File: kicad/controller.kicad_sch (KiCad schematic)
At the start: 25 parts, among them U1 RP2040, U2 W25Q16JVUXIQ, Y1 Crystal_GND24

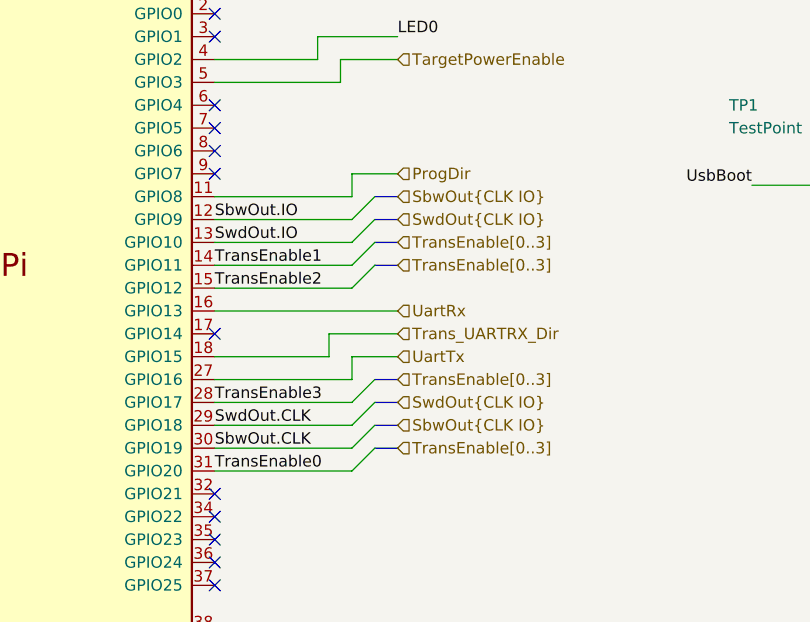
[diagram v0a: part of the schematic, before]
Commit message: add fourth level converter for simultaneous programming + TX/RX
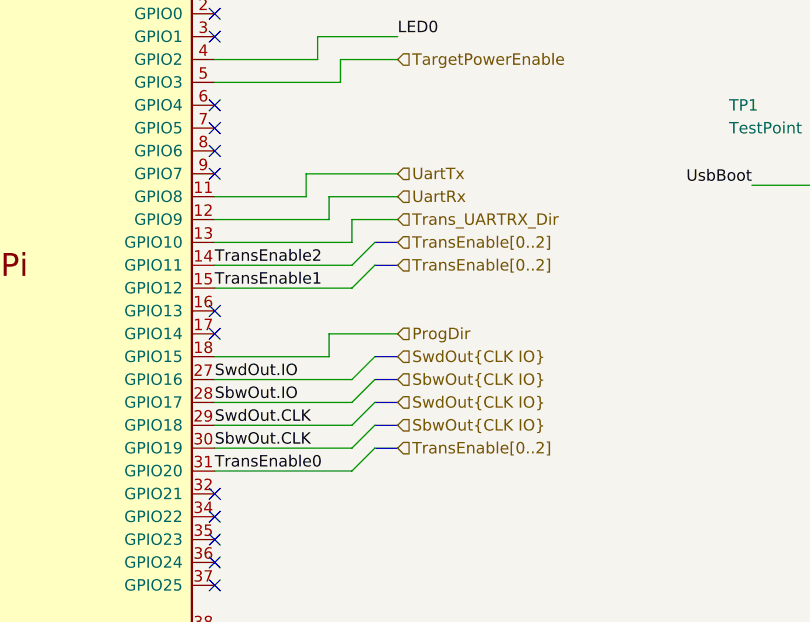
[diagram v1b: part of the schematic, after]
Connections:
- net TransEnable3 is gone; now on net SbwOut.IO: U1.28 (GPIO17)
- net ProgDir: now also U1.18 (GPIO15); no longer U1.11 (GPIO8)
- net SbwOut.IO: no longer U1.12 (GPIO9)
- net SwdOut.IO: now also U1.27 (GPIO16); no longer U1.13 (GPIO10)
- net TransEnable1: now also U1.15 (GPIO12); no longer U1.14 (GPIO11)
- net TransEnable2: now also U1.14 (GPIO11); no longer U1.15 (GPIO12)
- net Trans_UARTRX_Dir: now also U1.13 (GPIO10); no longer U1.18 (GPIO15)
- net UartRx: now also U1.12 (GPIO9); no longer U1.16 (GPIO13)
- net UartTx: now also U1.11 (GPIO8); no longer U1.27 (GPIO16)
- no-connect marks 19 -> 20

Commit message: replace target supply diode with analog switch
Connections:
- net LED0: now also U1.3 (GPIO1); no longer U1.4 (GPIO2)
- net TargetPowerEnable: now also U1.4 (GPIO2); no longer U1.5 (GPIO3)
- net PiGpio2: now reaches U1.37 (GPIO25)
- net PiGpio3: now reaches U1.38 (GPIO26_ADC0)
- net PiGpio0: now reaches U1.6 (GPIO4)
- net PiGpio1: now reaches U1.8 (GPIO6)
- no-connect marks 20 -> 16
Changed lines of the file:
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@@
   (junction (at 135.89 62.23) (diameter 0) (color 0 0 0 0)
   )
-  (no_connect (at 151.13 97.79))
   (no_connect (at 151.13 166.37))
-  (no_connect (at 151.13 110.49))
+  (no_connect (at 151.13 113.03))
   (no_connect (at 151.13 107.95))
   (no_connect (at 87.63 162.56))
@@
   (no_connect (at 151.13 148.59))
   (no_connect (at 151.13 171.45))
-  (no_connect (at 151.13 163.83))
   (no_connect (at 87.63 148.59))
-  (no_connect (at 151.13 113.03))
   (no_connect (at 87.63 160.02))
   (no_connect (at 151.13 153.67))
   (no_connect (at 151.13 95.25))
+  (no_connect (at 151.13 102.87))
   (no_connect (at 151.13 168.91))
   (no_connect (at 151.13 151.13))
-  (no_connect (at 151.13 158.75))
-  (no_connect (at 151.13 105.41))
   (no_connect (at 151.13 128.27))
   (no_connect (at 151.13 156.21))
@@
     (stroke (width 0) (type default) (color 0 0 0 0))
   )
+  (bus_entry (at 168.91 156.21) (size -2.54 2.54)
+    (stroke (width 0) (type default) (color 0 0 0 0))
+  )
   (bus_entry (at 168.91 120.65) (size -2.54 2.54)
     (stroke (width 0) (type default) (color 0 0 0 0))
   )
+  (bus_entry (at 168.91 107.95) (size -2.54 2.54)
+    (stroke (width 0) (type default) (color 0 0 0 0))
+  )
   (bus_entry (at 168.91 123.19) (size -2.54 2.54)
     (stroke (width 0) (type default) (color 0 0 0 0))
@@
     (stroke (width 0) (type default) (color 0 0 0 0))
   )
+  (bus_entry (at 168.91 161.29) (size -2.54 2.54)
+    (stroke (width 0) (type default) (color 0 0 0 0))
+  )
+  (bus_entry (at 168.91 102.87) (size -2.54 2.54)
+    (stroke (width 0) (type default) (color 0 0 0 0))
+  )
   (bus_entry (at 168.91 138.43) (size -2.54 2.54)
     (stroke (width 0) (type default) (color 0 0 0 0))
@@
     (stroke (width 0) (type default) (color 0 0 0 0))
   )
+  (wire (pts (xy 151.13 158.75) (xy 166.37 158.75))
+    (stroke (width 0) (type default) (color 0 0 0 0))
+  )
   (wire (pts (xy 166.37 118.11) (xy 171.45 118.11))
     (stroke (width 0) (type default) (color 0 0 0 0))
@@
     (stroke (width 0) (type default) (color 0 0 0 0))
   )
-  (wire (pts (xy 162.56 97.79) (xy 162.56 100.33))
-    (stroke (width 0) (type default) (color 0 0 0 0))
-  )
   (wire (pts (xy 101.6 77.47) (xy 101.6 68.58))
     (stroke (width 0) (type default) (color 0 0 0 0))
@@
     (stroke (width 0) (type default) (color 0 0 0 0))
   )
+  (wire (pts (xy 151.13 163.83) (xy 166.37 163.83))
+    (stroke (width 0) (type default) (color 0 0 0 0))
+  )
   (wire (pts (xy 256.54 95.25) (xy 256.54 106.68))
     (stroke (width 0) (type default) (color 0 0 0 0))
@@
     (stroke (width 0) (type default) (color 0 0 0 0))
   )
+  (wire (pts (xy 151.13 110.49) (xy 166.37 110.49))
+    (stroke (width 0) (type default) (color 0 0 0 0))
+  )
   (wire (pts (xy 43.18 129.54) (xy 39.37 129.54))
     (stroke (width 0) (type default) (color 0 0 0 0))
@@
     (stroke (width 0) (type default) (color 0 0 0 0))
   )
+  (wire (pts (xy 151.13 100.33) (xy 171.45 100.33))
+    (stroke (width 0) (type default) (color 0 0 0 0))
+  )
   (wire (pts (xy 151.13 135.89) (xy 166.37 135.89))
     (stroke (width 0) (type default) (color 0 0 0 0))
@@
     (stroke (width 0) (type default) (color 0 0 0 0))
   )
+  (bus (pts (xy 168.91 102.87) (xy 171.45 102.87))
+    (stroke (width 0) (type default) (color 0 0 0 0))
+  )
   (wire (pts (xy 152.4 57.15) (xy 152.4 58.42))
     (stroke (width 0) (type default) (color 0 0 0 0))
@@
     (stroke (width 0) (type default) (color 0 0 0 0))
   )
+  (bus (pts (xy 168.91 156.21) (xy 168.91 161.29))
+    (stroke (width 0) (type default) (color 0 0 0 0))
+  )
   (wire (pts (xy 123.19 69.85) (xy 125.73 69.85))
     (stroke (width 0) (type default) (color 0 0 0 0))
@@
     (stroke (width 0) (type default) (color 0 0 0 0))
   )
+  (wire (pts (xy 151.13 97.79) (xy 171.45 97.79))
+    (stroke (width 0) (type default) (color 0 0 0 0))
+  )
   (wire (pts (xy 241.3 114.3) (xy 243.84 114.3))
     (stroke (width 0) (type default) (color 0 0 0 0))
@@
     (stroke (width 0) (type default) (color 0 0 0 0))
   )
-  (wire (pts (xy 151.13 102.87) (xy 165.1 102.87))
-    (stroke (width 0) (type default) (color 0 0 0 0))
-  )
   (bus (pts (xy 168.91 133.35) (xy 171.45 133.35))
     (stroke (width 0) (type default) (color 0 0 0 0))
@@
     (stroke (width 0) (type default) (color 0 0 0 0))
   )
-  (wire (pts (xy 171.45 97.79) (xy 162.56 97.79))
-    (stroke (width 0) (type default) (color 0 0 0 0))
-  )
   (wire (pts (xy 246.38 46.99) (xy 246.38 48.26))
     (stroke (width 0) (type default) (color 0 0 0 0))
@@
     (stroke (width 0) (type default) (color 0 0 0 0))
   )
+  (bus (pts (xy 168.91 156.21) (xy 171.45 156.21))
+    (stroke (width 0) (type default) (color 0 0 0 0))
+  )
   (wire (pts (xy 228.6 114.3) (xy 241.3 114.3))
     (stroke (width 0) (type default) (color 0 0 0 0))
@@
     (stroke (width 0) (type default) (color 0 0 0 0))
   )
-  (wire (pts (xy 151.13 100.33) (xy 162.56 100.33))
-    (stroke (width 0) (type default) (color 0 0 0 0))
-  )
   (wire (pts (xy 163.83 130.81) (xy 163.83 133.35))
     (stroke (width 0) (type default) (color 0 0 0 0))
@@
     (stroke (width 0) (type default) (color 0 0 0 0))
   )
-  (wire (pts (xy 171.45 100.33) (xy 165.1 100.33))
-    (stroke (width 0) (type default) (color 0 0 0 0))
-  )
   (bus (pts (xy 168.91 138.43) (xy 171.45 138.43))
     (stroke (width 0) (type default) (color 0 0 0 0))
@@
     (stroke (width 0) (type default) (color 0 0 0 0))
   )
+  (bus (pts (xy 168.91 102.87) (xy 168.91 107.95))
+    (stroke (width 0) (type default) (color 0 0 0 0))
+  )
   (wire (pts (xy 203.2 48.26) (xy 193.04 48.26))
     (stroke (width 0) (type default) (color 0 0 0 0))
@@
     (stroke (width 0) (type default) (color 0 0 0 0))
   )
+  (wire (pts (xy 151.13 105.41) (xy 166.37 105.41))
+    (stroke (width 0) (type default) (color 0 0 0 0))
+  )
   (wire (pts (xy 82.55 107.95) (xy 87.63 107.95))
     (stroke (width 0) (type default) (color 0 0 0 0))
@@
     (stroke (width 0) (type default) (color 0 0 0 0))
   )
-  (wire (pts (xy 165.1 100.33) (xy 165.1 102.87))
-    (stroke (width 0) (type default) (color 0 0 0 0))
-  )
   (wire (pts (xy 162.56 58.42) (xy 172.72 58.42))
     (stroke (width 0) (type default) (color 0 0 0 0))
@@
     (effects (font (size 1.27 1.27)) (justify right bottom))
   )
+  (label "PiGpio3" (at 151.13 163.83 0)
+    (effects (font (size 1.27 1.27)) (justify left bottom))
+  )
+  (label "PiGpio0" (at 151.13 105.41 0)
+    (effects (font (size 1.27 1.27)) (justify left bottom))
+  )
   (label "TransEnable0" (at 151.13 146.05 0)
     (effects (font (size 1.27 1.27)) (justify left bottom))
@@
     (effects (font (size 1.27 1.27)) (justify right bottom))
   )
+  (label "PiGpio2" (at 151.13 158.75 0)
+    (effects (font (size 1.27 1.27)) (justify left bottom))
+  )
   (label "QSPI_SD0" (at 82.55 100.33 180)
     (effects (font (size 1.27 1.27)) (justify right bottom))
@@
     (effects (font (size 1.27 1.27)) (justify right bottom))
   )
+  (label "PiGpio1" (at 151.13 110.49 0)
+    (effects (font (size 1.27 1.27)) (justify left bottom))
+  )
+  (hierarchical_label "PiGpio[0..3]" (shape input) (at 171.45 102.87 0)
+    (effects (font (size 1.27 1.27)) (justify left))
+  )
   (hierarchical_label "UartTx" (shape input) (at 171.45 113.03 0)
     (effects (font (size 1.27 1.27)) (justify left))
@@
     (effects (font (size 1.27 1.27)) (justify left))
   )
+  (hierarchical_label "PiGpio[0..3]" (shape input) (at 171.45 156.21 0)
+    (effects (font (size 1.27 1.27)) (justify left))
+  )

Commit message: add MPNs in schematics
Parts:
- C1, C2: MPN (none) -> 04025A120JAT2A
- C10, C11, C12, C13, C14, C3, C4, C6, C8, C9: MPN (none) -> CL05A104KA5NNNC
- C5, C7: MPN (none) -> CL05A475MP5NRNC
- D1: MPN (none) -> QBLP595-AG1
- R1, R4: MPN (none) -> WR04X1001FTL
- R2, R3: MPN (none) -> CR0402-FX-27R0GLF
- R6: MPN (none) -> CR0402-FX-1200GLF
- U1: MPN (none) -> RP2040-7
- U2: MPN (none) -> W25Q16JVUXIQ
- Y1: MPN (none) -> RH100-12.000-18-2030-TR
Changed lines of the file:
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@@
+      (effects (font (size 1.27 1.27)) hide)
+    )
+    (property "MPN" "CL05A104KA5NNNC" (id 4) (at 142.24 53.34 0)
       (effects (font (size 1.27 1.27)) hide)
     )
@@
       (effects (font (size 1.27 1.27)) hide)
     )
+    (property "MPN" "CR0402-FX-27R0GLF" (id 4) (at 166.37 87.63 0)
+      (effects (font (size 1.27 1.27)) hide)
+    )
     (pin "1")
     (pin "2")
@@
     )
     (property "Datasheet" "~" (id 3) (at 246.38 52.07 0)
+      (effects (font (size 1.27 1.27)) hide)
+    )
+    (property "MPN" "QBLP595-AG1" (id 4) (at 246.38 52.07 0)
       (effects (font (size 1.27 1.27)) hide)
     )
@@
       (effects (font (size 1.27 1.27)) hide)
     )
+    (property "MPN" "RH100-12.000-18-2030-TR" (id 4) (at 48.26 129.54 0)
+      (effects (font (size 1.27 1.27)) hide)
+    )
     (pin "1")
     (pin "2")
@@
     )
     (property "Datasheet" "" (id 3) (at 100.33 128.27 0)
+      (effects (font (size 1.27 1.27)) hide)
+    )
+    (property "MPN" "RP2040-7" (id 4) (at 119.38 128.27 0)
       (effects (font (size 1.27 1.27)) hide)
     )
@@
       (effects (font (size 1.27 1.27)) hide)
     )
+    (property "MPN" "CL05A104KA5NNNC" (id 4) (at 81.28 53.34 0)
+      (effects (font (size 1.27 1.27)) hide)
+    )
     (pin "1")
     (pin "2")
@@
     )
     (property "Datasheet" "~" (id 3) (at 91.44 53.34 0)
+      (effects (font (size 1.27 1.27)) hide)
+    )
+    (property "MPN" "CL05A104KA5NNNC" (id 4) (at 91.44 53.34 0)
       (effects (font (size 1.27 1.27)) hide)
     )
@@
       (effects (font (size 1.27 1.27)) hide)
     )
+    (property "MPN" "CL05A104KA5NNNC" (id 4) (at 193.04 53.34 0)
+      (effects (font (size 1.27 1.27)) hide)
+    )
     (pin "1")
     (pin "2")
@@
       (effects (font (size 1.27 1.27)) hide)
     )
+    (property "MPN" "04025A120JAT2A" (id 4) (at 31.75 123.19 0)
+      (effects (font (size 1.27 1.27)) hide)
+    )
     (pin "1")
     (pin "2")
@@
     )
     (property "Datasheet" "~" (id 3) (at 91.44 67.31 0)
+      (effects (font (size 1.27 1.27)) hide)
+    )
+    (property "MPN" "CL05A475MP5NRNC" (id 4) (at 91.44 67.31 0)
       (effects (font (size 1.27 1.27)) hide)
     )
@@
     )
     (property "Datasheet" "https://www.winbond.com/resource-files/w25q16jv%20spi%20revh%2004082019%20plus.pdf" (id 3) (at 257.81 139.7 0)
+      (effects (font (size 1.27 1.27)) hide)
+    )
+    (property "MPN" "W25Q16JVUXIQ" (id 4) (at 256.54 116.84 0)
       (effects (font (size 1.27 1.27)) hide)
     )
@@
       (effects (font (size 1.27 1.27)) hide)
     )
+    (property "MPN" "CL05A104KA5NNNC" (id 4) (at 172.72 53.34 0)
+      (effects (font (size 1.27 1.27)) hide)
+    )
     (pin "1")
     (pin "2")
@@
     )
     (property "Datasheet" "~" (id 3) (at 162.56 53.34 0)
+      (effects (font (size 1.27 1.27)) hide)
+    )
+    (property "MPN" "CL05A104KA5NNNC" (id 4) (at 162.56 53.34 0)
       (effects (font (size 1.27 1.27)) hide)
     )
@@
       (effects (font (size 1.27 1.27)) hide)
     )
+    (property "MPN" "WR04X1001FTL" (id 4) (at 224.79 114.3 0)
+      (effects (font (size 1.27 1.27)) hide)
+    )
     (pin "1")
     (pin "2")
@@
       (effects (font (size 1.27 1.27)) hide)
     )
+    (property "MPN" "04025A120JAT2A" (id 4) (at 31.75 135.89 0)
+      (effects (font (size 1.27 1.27)) hide)
+    )
     (pin "1")
     (pin "2")
@@
       (effects (font (size 1.27 1.27)) hide)
     )
+    (property "MPN" "CL05A104KA5NNNC" (id 4) (at 182.88 53.34 0)
+      (effects (font (size 1.27 1.27)) hide)
+    )
     (pin "1")
     (pin "2")
@@
       (effects (font (size 1.27 1.27)) hide)
     )
+    (property "MPN" "CL05A104KA5NNNC" (id 4) (at 262.89 96.52 0)
+      (effects (font (size 1.27 1.27)) hide)
+    )
     (pin "1")
     (pin "2")
@@
     )
     (property "Datasheet" "~" (id 3) (at 142.24 67.31 0)
+      (effects (font (size 1.27 1.27)) hide)
+    )
+    (property "MPN" "CL05A475MP5NRNC" (id 4) (at 142.24 67.31 0)
       (effects (font (size 1.27 1.27)) hide)
     )
@@
       (effects (font (size 1.27 1.27)) hide)
     )
+    (property "MPN" "WR04X1001FTL" (id 4) (at 68.58 135.89 0)
+      (effects (font (size 1.27 1.27)) hide)
+    )
     (pin "1")
     (pin "2")
@@
     )
     (property "Datasheet" "~" (id 3) (at 246.38 43.18 0)
+      (effects (font (size 1.27 1.27)) hide)
+    )
+    (property "MPN" "CR0402-FX-1200GLF" (id 4) (at 246.38 43.18 0)
       (effects (font (size 1.27 1.27)) hide)
     )
@@
       (effects (font (size 1.27 1.27)) hide)
     )
+    (property "MPN" "CR0402-FX-27R0GLF" (id 4) (at 166.37 78.74 0)
+      (effects (font (size 1.27 1.27)) hide)
+    )
     (pin "1")
     (pin "2")
@@
       (effects (font (size 1.27 1.27)) hide)
     )
+    (property "MPN" "CL05A104KA5NNNC" (id 4) (at 152.4 53.34 0)
+      (effects (font (size 1.27 1.27)) hide)
+    )
     (pin "1")
     (pin "2")
@@
       (effects (font (size 1.27 1.27)) hide)
     )
+    (property "MPN" "CL05A104KA5NNNC" (id 4) (at 203.2 53.34 0)
+      (effects (font (size 1.27 1.27)) hide)
+    )

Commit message: update footprints and add component description to BOM
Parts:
- U1: MPN RP2040-7 -> RP2040
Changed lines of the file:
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@@
+      (effects (font (size 1.27 1.27)) hide)
+    )
+    (property "Description" "Cap, 0402, X5R/X7R, 10V" (id 5) (at 142.24 53.34 0)
       (effects (font (size 1.27 1.27)) hide)
     )
@@
       (effects (font (size 1.27 1.27)) hide)
     )
+    (property "Description" "Res, 0402, 1%" (id 5) (at 166.37 87.63 0)
+      (effects (font (size 1.27 1.27)) hide)
+    )
     (pin "1")
     (pin "2")
@@
     )
     (property "MPN" "QBLP595-AG1" (id 4) (at 246.38 52.07 0)
+      (effects (font (size 1.27 1.27)) hide)
+    )
+    (property "Description" "LED, 0402, green, clear" (id 5) (at 246.38 52.07 0)
       (effects (font (size 1.27 1.27)) hide)
     )
@@
       (effects (font (size 1.27 1.27)) hide)
     )
+    (property "Description" "12MHZ 18PF Crystal" (id 5) (at 48.26 129.54 0)
+      (effects (font (size 1.27 1.27)) hide)
+    )
     (pin "1")
     (pin "2")
@@
       (effects (font (size 1.27 1.27)) hide)
     )
-    (property "MPN" "RP2040-7" (id 4) (at 119.38 128.27 0)
+    (property "MPN" "RP2040" (id 4) (at 119.38 128.27 0)
+      (effects (font (size 1.27 1.27)) hide)
+    )
+    (property "Description" "" (id 5) (at 119.38 128.27 0)
       (effects (font (size 1.27 1.27)) hide)
     )
@@
       (effects (font (size 1.27 1.27)) hide)
     )
+    (property "Description" "Cap, 0402, X5R/X7R, 10V" (id 5) (at 81.28 53.34 0)
+      (effects (font (size 1.27 1.27)) hide)
+    )
     (pin "1")
     (pin "2")
@@
     )
     (property "MPN" "CL05A104KA5NNNC" (id 4) (at 91.44 53.34 0)
+      (effects (font (size 1.27 1.27)) hide)
+    )
+    (property "Description" "Cap, 0402, X5R/X7R, 10V" (id 5) (at 91.44 53.34 0)
       (effects (font (size 1.27 1.27)) hide)
     )
@@
       (effects (font (size 1.27 1.27)) hide)
     )
+    (property "Description" "Cap, 0402, X5R/X7R, 10V" (id 5) (at 193.04 53.34 0)
+      (effects (font (size 1.27 1.27)) hide)
+    )
     (pin "1")
     (pin "2")
@@
       (effects (font (size 1.27 1.27)) hide)
     )
+    (property "Description" "Cap, 0402, C0G/NP0, 50V" (id 5) (at 31.75 123.19 0)
+      (effects (font (size 1.27 1.27)) hide)
+    )
     (pin "1")
     (pin "2")
@@
     )
     (property "MPN" "CL05A475MP5NRNC" (id 4) (at 91.44 67.31 0)
+      (effects (font (size 1.27 1.27)) hide)
+    )
+    (property "Description" "Cap, 0402, X5R/X7R, 10V" (id 5) (at 91.44 67.31 0)
       (effects (font (size 1.27 1.27)) hide)
     )
@@
     )
     (property "MPN" "W25Q16JVUXIQ" (id 4) (at 256.54 116.84 0)
+      (effects (font (size 1.27 1.27)) hide)
+    )
+    (property "Description" "16Mbi SPI NOR flash" (id 5) (at 256.54 116.84 0)
       (effects (font (size 1.27 1.27)) hide)
     )
@@
       (effects (font (size 1.27 1.27)) hide)
     )
+    (property "Description" "Cap, 0402, X5R/X7R, 10V" (id 5) (at 172.72 53.34 0)
+      (effects (font (size 1.27 1.27)) hide)
+    )
     (pin "1")
     (pin "2")
@@
     )
     (property "MPN" "CL05A104KA5NNNC" (id 4) (at 162.56 53.34 0)
+      (effects (font (size 1.27 1.27)) hide)
+    )
+    (property "Description" "Cap, 0402, X5R/X7R, 10V" (id 5) (at 162.56 53.34 0)
       (effects (font (size 1.27 1.27)) hide)
     )
@@
       (effects (font (size 1.27 1.27)) hide)
     )
+    (property "Description" "Res, 0402, 1%" (id 5) (at 224.79 114.3 0)
+      (effects (font (size 1.27 1.27)) hide)
+    )
     (pin "1")
     (pin "2")
@@
       (effects (font (size 1.27 1.27)) hide)
     )
+    (property "Description" "Cap, 0402, C0G/NP0, 50V" (id 5) (at 31.75 135.89 0)
+      (effects (font (size 1.27 1.27)) hide)
+    )
     (pin "1")
     (pin "2")
@@
       (effects (font (size 1.27 1.27)) hide)
     )
+    (property "Description" "Cap, 0402, X5R/X7R, 10V" (id 5) (at 182.88 53.34 0)
+      (effects (font (size 1.27 1.27)) hide)
+    )
     (pin "1")
     (pin "2")
@@
       (effects (font (size 1.27 1.27)) hide)
     )
+    (property "Description" "Cap, 0402, X5R/X7R, 10V" (id 5) (at 262.89 96.52 0)
+      (effects (font (size 1.27 1.27)) hide)
+    )
     (pin "1")
     (pin "2")
@@
     )
     (property "MPN" "CL05A475MP5NRNC" (id 4) (at 142.24 67.31 0)
+      (effects (font (size 1.27 1.27)) hide)
+    )
+    (property "Description" "Cap, 0402, X5R/X7R, 10V" (id 5) (at 142.24 67.31 0)
       (effects (font (size 1.27 1.27)) hide)
     )
@@
       (effects (font (size 1.27 1.27)) hide)
     )
+    (property "Description" "Res, 0402, 1%" (id 5) (at 68.58 135.89 0)
+      (effects (font (size 1.27 1.27)) hide)
+    )
     (pin "1")
     (pin "2")
@@
     )
     (property "MPN" "CR0402-FX-1200GLF" (id 4) (at 246.38 43.18 0)
+      (effects (font (size 1.27 1.27)) hide)
+    )
+    (property "Description" "Res, 0402, 1%" (id 5) (at 246.38 43.18 0)
       (effects (font (size 1.27 1.27)) hide)
     )
@@
       (effects (font (size 1.27 1.27)) hide)
     )
+    (property "Description" "Res, 0402, 1%" (id 5) (at 166.37 78.74 0)
+      (effects (font (size 1.27 1.27)) hide)
+    )
     (pin "1")
     (pin "2")
@@
       (effects (font (size 1.27 1.27)) hide)
     )
+    (property "Description" "Cap, 0402, X5R/X7R, 10V" (id 5) (at 152.4 53.34 0)
+      (effects (font (size 1.27 1.27)) hide)
+    )
     (pin "1")
     (pin "2")
@@
       (effects (font (size 1.27 1.27)) hide)
     )
+    (property "Description" "Cap, 0402, X5R/X7R, 10V" (id 5) (at 203.2 53.34 0)
+      (effects (font (size 1.27 1.27)) hide)
+    )

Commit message: add conformity marks and refine BOM settings
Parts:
- R5: now in the parts list
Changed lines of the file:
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@@
   )
   (symbol (lib_id "Device:R") (at 241.3 102.87 0) (unit 1)
-    (in_bom no) (on_board yes) (fields_autoplaced)
+    (in_bom yes) (on_board yes) (fields_autoplaced)
     (property "Reference" "R5" (id 0) (at 243.078 102.0353 0)
       (effects (font (size 1.27 1.27)) (justify left))
